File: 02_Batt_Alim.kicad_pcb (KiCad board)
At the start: 2 copper layers, 29.2 x 25.4 mm, 28 parts, among them IC1 TP4056, J1 Conn_01x01, J2 Conn_01x01, J3 Conn_01x01, J9 Conn_01x01, U1 ME2108A50M3

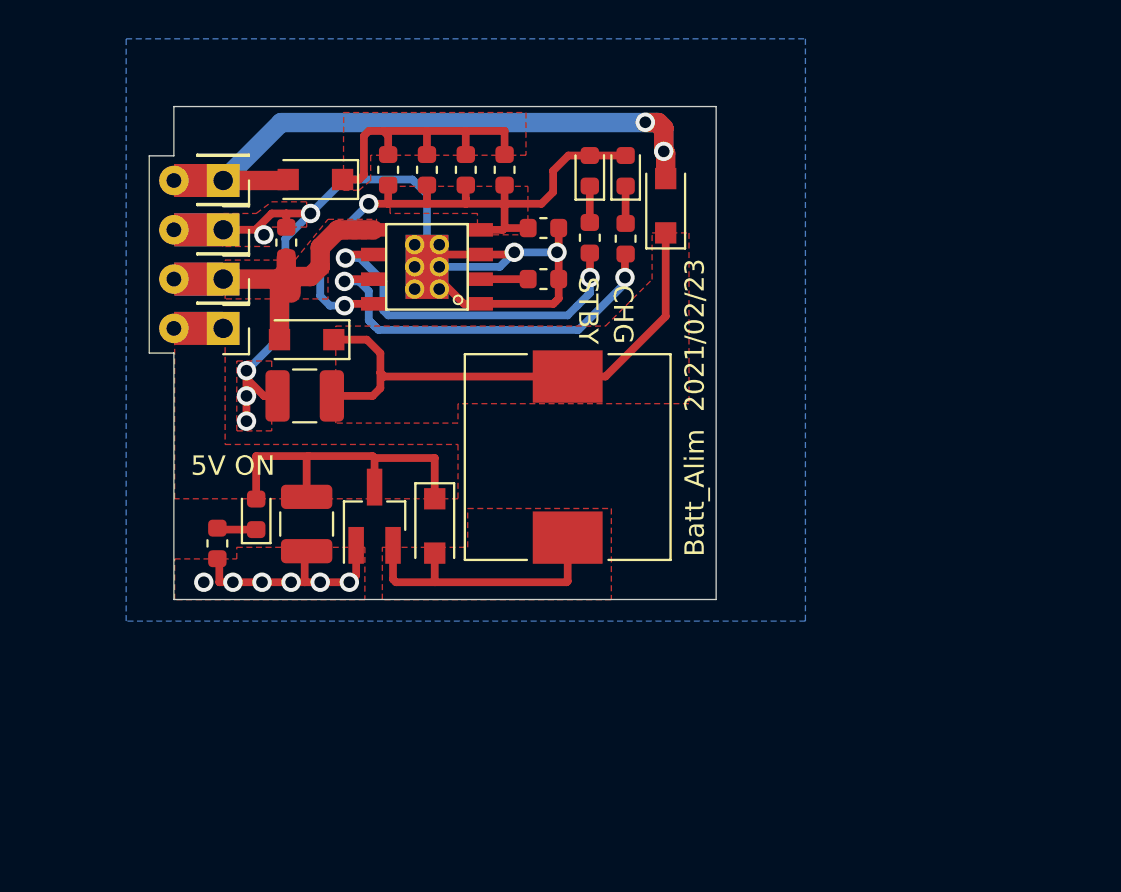
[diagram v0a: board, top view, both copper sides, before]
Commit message: coupé en deux
séparé la partie dcdc du chargeur;
schéma fait et routage en cours de modification
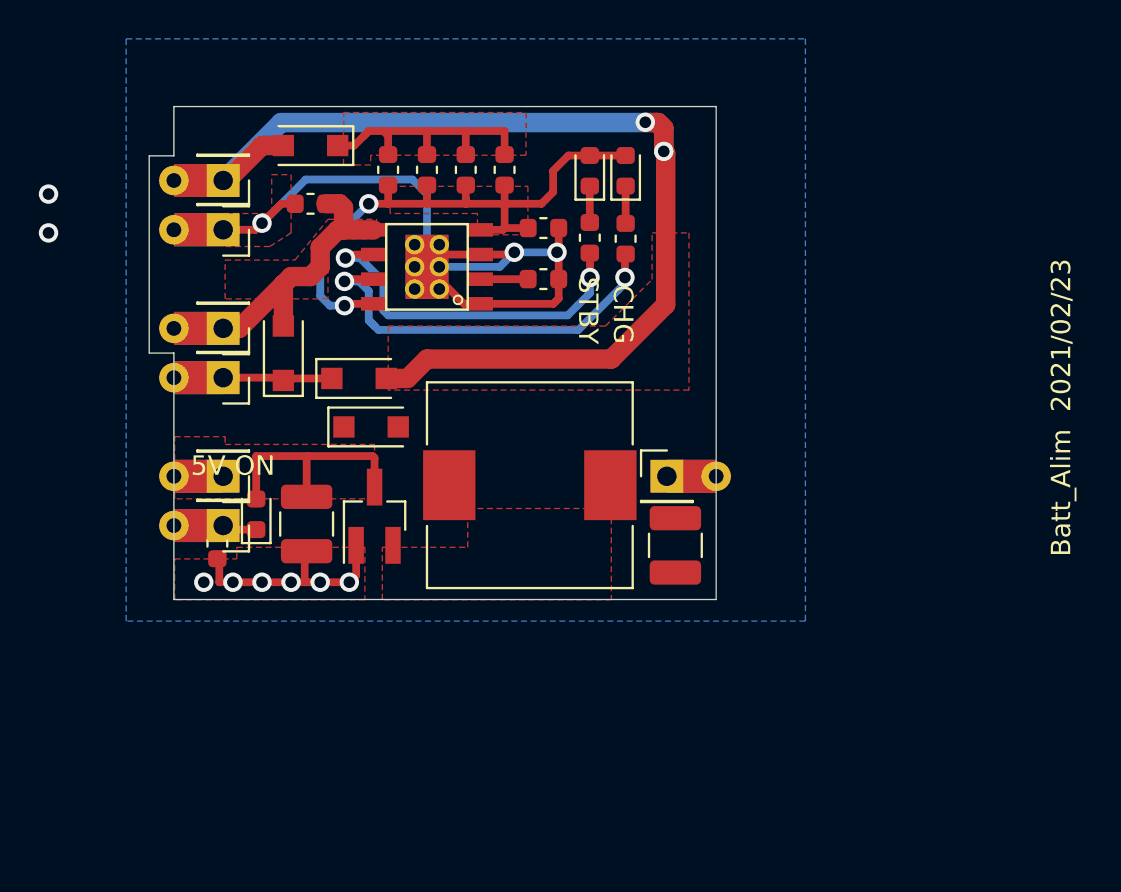
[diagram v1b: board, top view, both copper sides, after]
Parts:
- removed REF**: OSHW-Logo2_7.3x6mm_SilkScreen, Symbol:OSHW-Logo2_7.3x6mm_SilkScreen
- removed REF**: KiCad-Logo2_5mm_SilkScreen, Symbol:KiCad-Logo2_5mm_SilkScreen
- added J4: Conn_01x01, Chimere:Castellated_conn, F.Cu at (104.1, 76.2)
- added J5: Conn_01x01, Chimere:Castellated_conn, F.Cu at (127.0, 81.3)
- added J6: Conn_01x01, Chimere:Castellated_conn, F.Cu at (104.1, 83.8)
- moved C4 20.6 mm to (127.4, 84.8), turned to 270 degrees
- moved D4 18.1 mm to (111.1, 76.2), turned to 0 degrees
- moved J3 7.62 mm to (104.1, 81.3)
- moved D5 6.06 mm to (111.8, 78.7), turned to 0 degrees
- moved J9 2.54 mm to (104.1, 73.7)
- moved L1 2.43 mm to (119.9, 81.7), turned to 0 degrees
- moved C2 2.36 mm to (108.6, 67.2), turned to 0 degrees
- moved D7 1.77 mm to (108.6, 64.2)
- moved D8 1.39 mm to (107.2, 74.9), turned to 90 degrees
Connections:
- C4 pad 1: V_sum -> DCDC_IN
- L1 pad 2: V_sum -> DCDC_IN
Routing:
- net V_sum: track 27.5 -> 5.70 mm
- net V_ext: track 38.8 -> 60.5 mm
- net /LX: track 14.6 -> 0.00 mm
- net GND: track 70.7 -> 57.7 mm, vias 13 -> 11
- net 5V: track 17.2 -> 12.0 mm
- net /V_ext_p: track 15.5 -> 14.2 mm
- net V_BAT+: track 18.1 -> 17.3 mm
- added copper zone on F.Cu, net V_ext
- removed copper zone on F.Cu, net V_sum

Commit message: modifications
ajout diode + capa pour filtrer + protection en sortie
changement inductance
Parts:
- added C5: 47uF, Capacitor_SMD:C_1210_3225Metric, F.Cu at (105.9, 95.9)
- added D1: 1N5819W, Diode_SMD:D_SOD-123F, F.Cu at (105.8, 99.7)
- L1: value 33uH -> MWSA0603S-330MT; footprint Inductor_SMD:L_10.4x10.4_H4.8 -> Chimere:L_Sunlord_MWSA0603S_6.6x7.0x2.8mm
- moved D5 3.81 mm to (115.6, 78.7)
- moved L1 1.89 mm to (119.4, 83.5)
- moved C4 1.77 mm to (125.7, 85.3)
- moved J5 1.27 mm to (125.7, 81.3)
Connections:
- J3 pad 1: 5V -> 5V_p
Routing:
- net GND: track 57.7 -> 51.3 mm
- net V_ext: track 60.5 -> 55.2 mm
- net V_BAT+: track 17.3 -> 13.9 mm
- removed copper zone on F.Cu, net /LX

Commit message: routage
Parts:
- moved D1 19.8 mm to (109.3, 80.1)
- moved R15 17.2 mm to (119.6, 78.0), turned to 0 degrees
- moved C5 12.2 mm to (107.6, 83.7), turned to 270 degrees
- moved D6 11.7 mm to (116.3, 78.0), turned to 180 degrees
- moved C4 5.71 mm to (127.0, 79.7), turned to 90 degrees
- moved J5 2.84 mm to (127.0, 83.8)
- moved U1 2.66 mm to (114.4, 84.2)
- moved C3 2.50 mm to (110.9, 83.7)
- moved D5 1.74 mm to (114.5, 80.1)
- moved L1 1.37 mm to (120.7, 83.3)
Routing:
- net GND: track 51.3 -> 109.1 mm, vias 11 -> 13
- net /LX: track 0.00 -> 8.56 mm
- net 5V_p: track 0.00 -> 6.66 mm
- net DCDC_IN: track 0.00 -> 6.06 mm
- net 5V: track 12.0 -> 14.1 mm
- net V_ext: track 55.2 -> 56.1 mm
- added copper zone on F.Cu, net /LX
- added copper zone on F.Cu, net 5V_p
- added copper zone on F.Cu, net DCDC_IN
- added copper zone on F.Cu, net V_sum
- removed copper zone on F.Cu, net V_ext
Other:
- board size 29.2 x 25.4 mm -> 30.5 x 25.4 mm
- board text added: "+BAT"
- board text added: "Batt_Alim 2021/05/31"
- board text added: "DCDCIN"
- board text added: "Vext"
- board text added: "Vsum"
- board text removed: "Batt_Alim 2021/02/23"
